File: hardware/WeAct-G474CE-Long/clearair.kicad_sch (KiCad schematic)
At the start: 39 parts, among them J1 220VAC mains in, J2 STLINK-V3MINIE STDC14, J3 SPS30 wire header (1 VDD, 2 S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, J4 BME680 wire header (1 VCC, 2 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, J5 MQ131 wire header (1 VCC, 2 G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, J6 MiCS-4514 wire header (1 VCC,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, M1 AC vent fan, M2 80mm fan front, M3 80mm fan rear, Q1 2N7000, Q2 2N7000, Q3 2N2222A, SW1 RESET, SW2 COLD_BOOT, U5 RobotDyn AC dimmer, U6 PCF8563 RTC

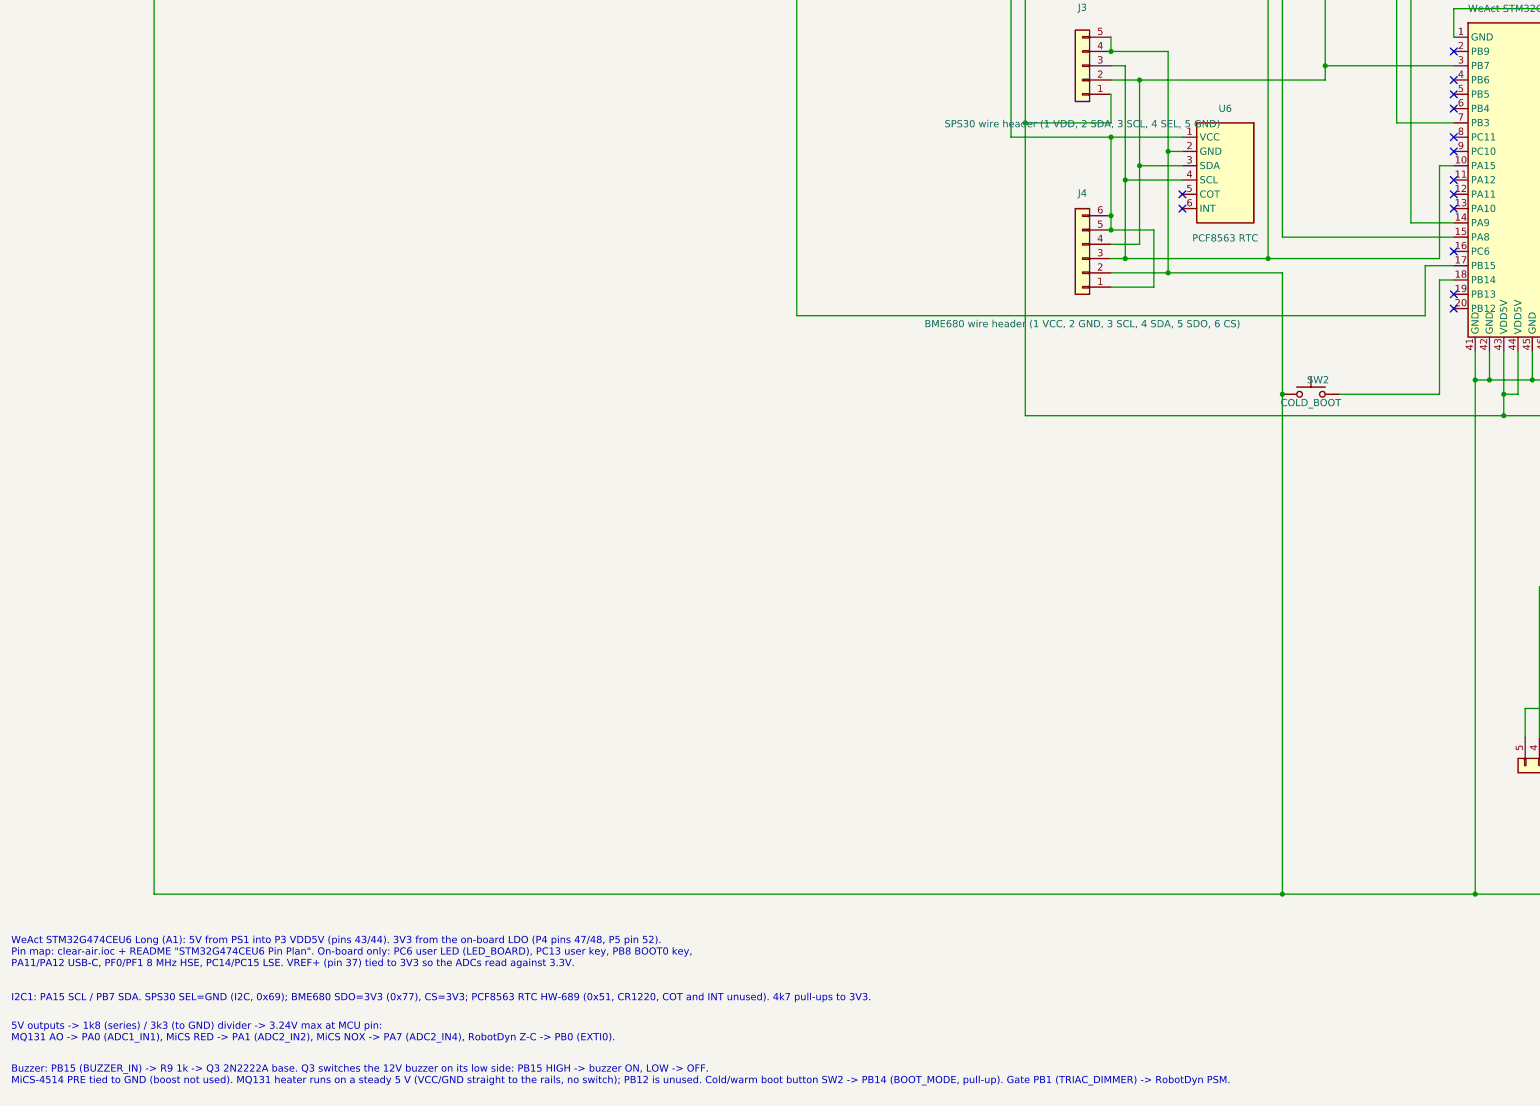
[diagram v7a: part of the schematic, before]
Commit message: split to 2 boards
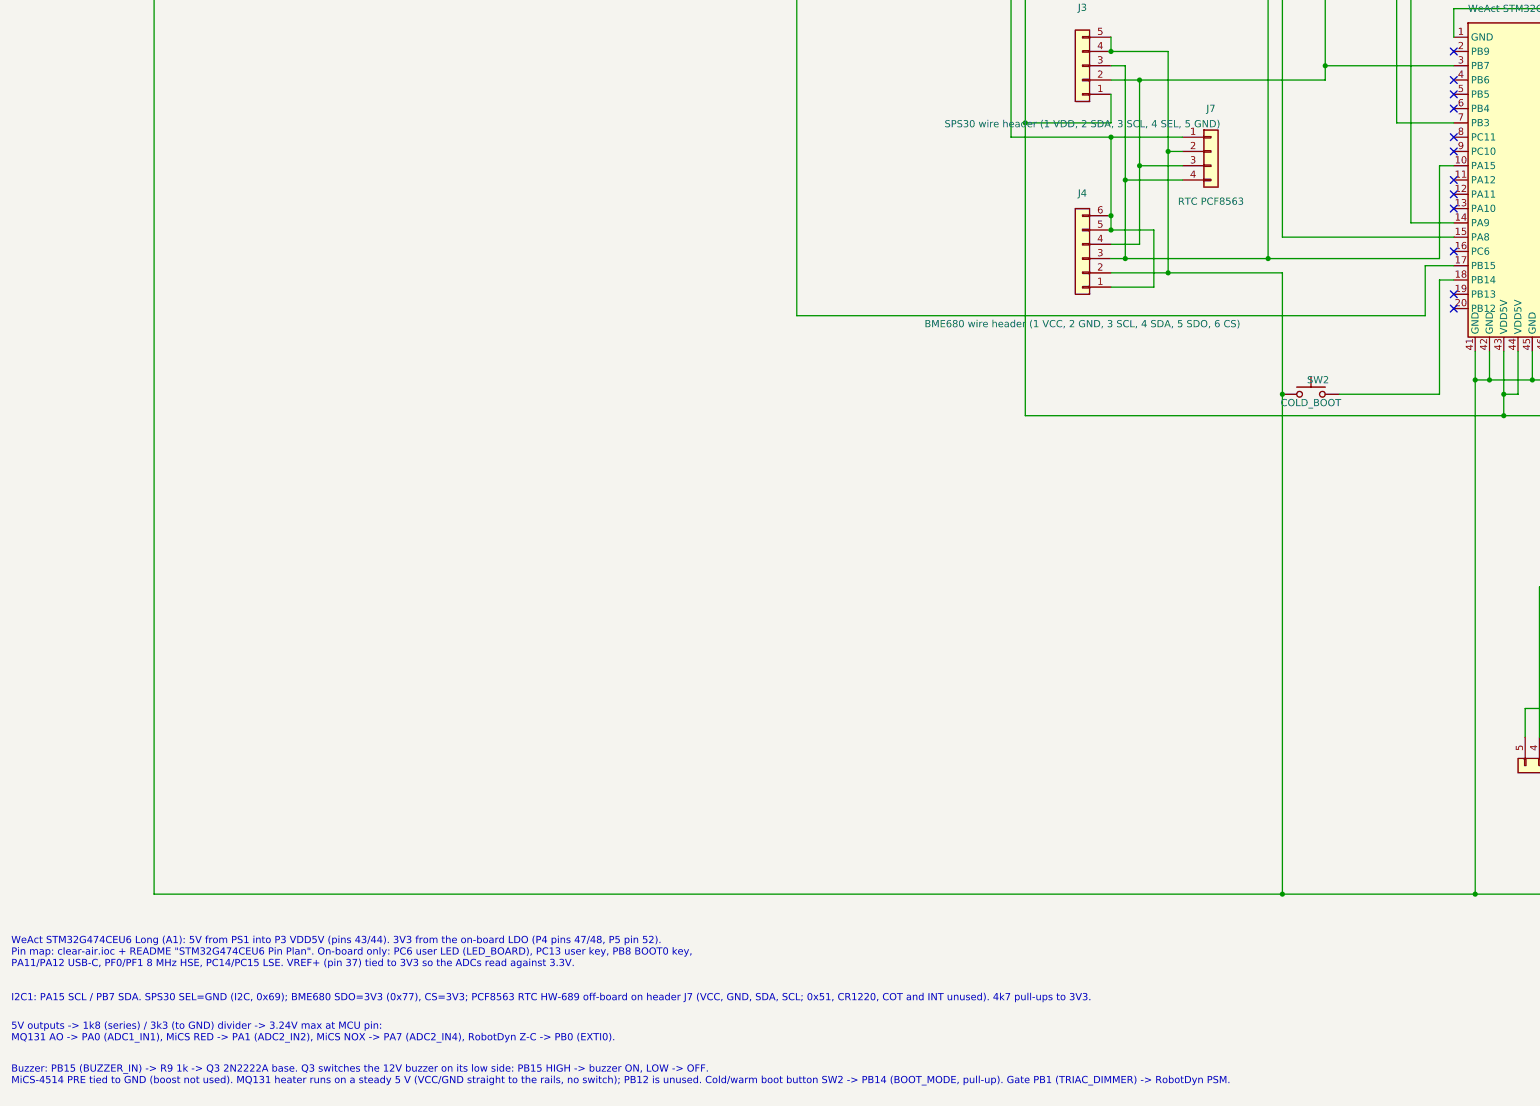
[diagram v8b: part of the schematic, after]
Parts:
- removed U6: PCF8563 RTC, libraries:PCF8563_HW689, symbol FullModules:PCF8563_HW689
- added J7: RTC PCF8563, Connector_PinHeader_2.54mm:PinHeader_1x04_P2.54mm_Vertical, symbol Connector_Generic:Conn_01x04
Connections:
- net +3V3: now also J7.1 (Pin_1)
- net GND: now also J7.2 (Pin_2)
- net at A1.10 (PA15), J3.3 (Pin_3), J4.3 (Pin_3)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: now also J7.4 (Pin_4)
- net at A1.3 (PB7), J3.2 (Pin_2), J4.4 (Pin_4)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: now also J7.3 (Pin_3)
- no-connect marks 52 -> 50
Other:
- note added: "I2C1: PA15 SCL / PB7 SDA. SPS30 SEL=GND (I2C, 0x69); BME680 SDO=3V3 (0x77), CS=3V3; PCF8563 RTC HW-689 off-board on header J7 (VCC, GND, SDA, SCL; 0x51, CR1220, COT and INT unused). 4k7 pull-ups to 3V3."
- note removed: "I2C1: PA15 SCL / PB7 SDA. SPS30 SEL=GND (I2C, 0x69); BME680 SDO=3V3 (0x77), CS=3V3; PCF8563 RTC HW-689 (0x51, CR1220, COT and INT unused). 4k7 pull-ups to 3V3."
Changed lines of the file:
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@@
 		(comment 2 "All pins wired point-to-point")
 	)
-	(text "I2C1: PA15 SCL / PB7 SDA. SPS30 SEL=GND (I2C, 0x69); BME680 SDO=3V3 (0x77), CS=3V3; PCF8563 RTC HW-689 (0x51, CR1220, COT and INT unused). 4k7 pull-ups to 3V3."
+	(text "I2C1: PA15 SCL / PB7 SDA. SPS30 SEL=GND (I2C, 0x69); BME680 SDO=3V3 (0x77), CS=3V3; PCF8563 RTC HW-689 off-board on header J7 (VCC, GND, SDA, SCL; 0x51, CR1220, COT and INT unused). 4k7 pull-ups to 3V3."
 		(exclude_from_sim no)
 		(at 25.4 345.44 0)
@@
 	)
 	(no_connect
-		(at 233.68 203.2)
-	)
-	(no_connect
 		(at 467.36 223.52)
 	)
@@
 	)
 	(no_connect
-		(at 233.68 205.74)
-	)
-	(no_connect
 		(at 281.94 213.36)
 	)
@@
 	)
 	(symbol
-		(lib_id "FullModules:PCF8563_HW689")
-		(at 238.76 199.39 270)
+		(lib_id "Connector_Generic:Conn_01x04")
+		(at 238.76 195.58 0)
 		(unit 1)
 		(body_style 1)
@@
 		(in_pos_files yes)
 		(dnp no)
-		(property "Reference" "U6"
-			(at 241.3 187.96 90)
-			(show_name no)
-			(do_not_autoplace no)
-			(effects
-				(font
-					(size 1.27 1.27)
-				)
-			)
-		)
-		(property "Value" "PCF8563 RTC"
-			(at 241.3 211 90)
+		(property "Reference" "J7"
+			(at 238.76 187.96 0)
 			(show_name no)
 			(do_not_autoplace no)
@@
 			)
 		)
-		(property "Footprint" "libraries:PCF8563_HW689"
-			(at 238.76 199.39 90)
-			(hide yes)
+		(property "Value" "RTC PCF8563"
+			(at 238.76 204.47 0)
 			(show_name no)
 			(do_not_autoplace no)
@@
 			)
 		)
-		(property "Datasheet" "https://www.nxp.com/docs/en/data-sheet/PCF8563.pdf"
-			(at 238.76 199.39 90)
+		(property "Footprint" "Connector_PinHeader_2.54mm:PinHeader_1x04_P2.54mm_Vertical"
+			(at 238.76 195.58 0)
 			(hide yes)
 			(show_name no)
@@
 			)
 		)
-		(property "Description" "PCF8563 real-time clock module, board marking HW-689 (43 x 17 mm), I2C address 0x51, 1.0-5.5 V. 6-pin header VCC/GND/SDA/SCL/COT/INT in the order printed on the board. COT is the programmable clock output, INT is the open-drain alarm/timer interrupt (needs a pull-up if used). CR1220 backup cell holder on board (12.5 mm cell, 3.5 mm deep). The photographed board seems to have no I2C pull-ups: add 4.7k to 3V3 on the bus."
-			(at 238.76 199.39 90)
+		(property "Datasheet" ""
+			(at 238.76 195.58 0)
 			(hide yes)
 			(show_name no)
@@
 			)
 		)
-		(property "ki_keywords" "PCF8563 HW-689 RTC real time clock I2C module CR1220"
-			(at 238.76 199.39 90)
+		(property "Description" "Header to the off-board PCF8563 RTC module HW-689: 1 VCC (3V3), 2 GND, 3 SDA, 4 SCL. COT and INT unused."
+			(at 238.76 195.58 0)
 			(hide yes)
 			(show_name no)
@@
 		(pin "4"
 		)
-		(pin "5"
-		)
-		(pin "6"
-		)
 		(instances
 			(project "clearair"
 				(path "/953560a5-36cf-5251-8f8d-509802d70a69"
-					(reference "U6")
+					(reference "J7")
 					(unit 1)
 				)
